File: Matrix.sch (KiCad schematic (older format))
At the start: 116 parts

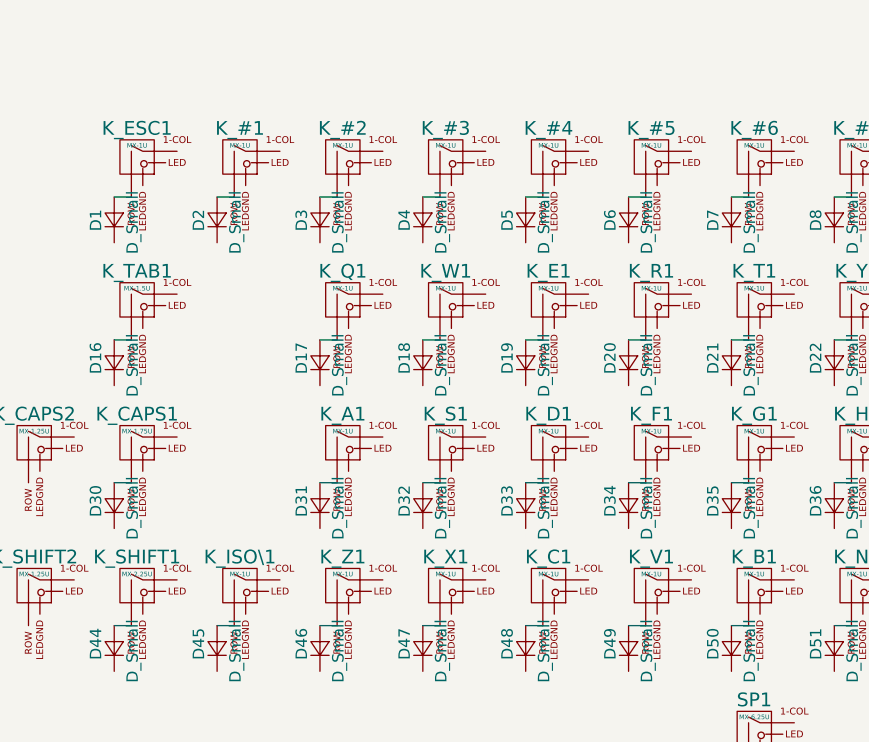
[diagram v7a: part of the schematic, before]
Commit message: Remove alps row
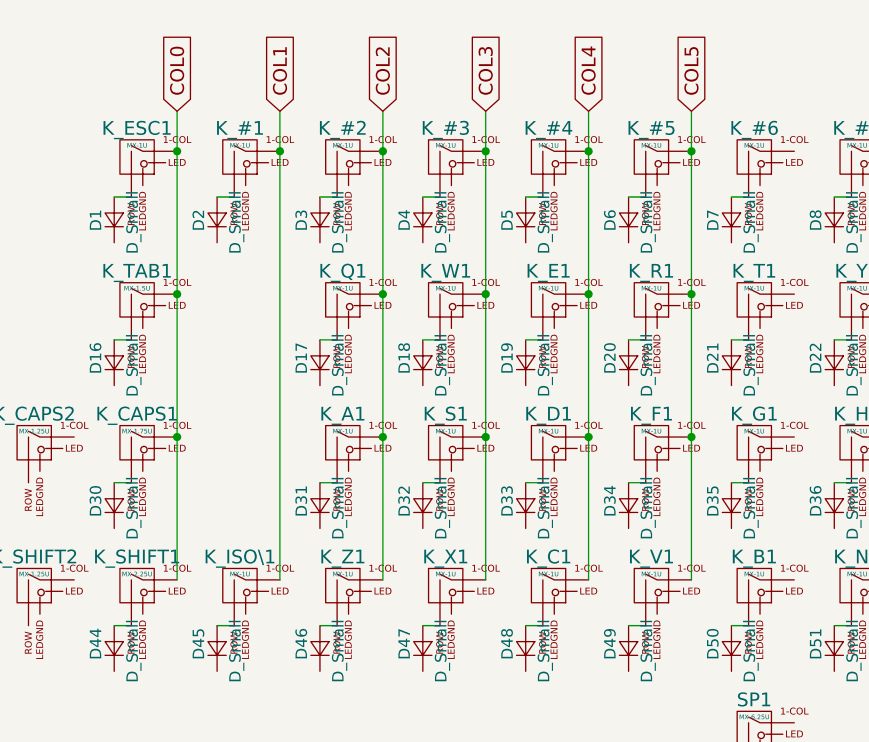
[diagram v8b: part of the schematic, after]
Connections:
- net COL0: now reaches K_ESC1.1 (COL)
- net COL0: now also K_CAPS1.1 (COL), K_SHIFT1.1 (COL), K_TAB1.1 (COL)
- net COL1: now reaches K_#1.1 (COL)
- net COL1: now also K_ISO\1.1 (COL)
- net COL2: now reaches K_#2.1 (COL)
- net COL2: now also K_A1.1 (COL), K_Q1.1 (COL), K_Z1.1 (COL)
- net COL3: now reaches K_#3.1 (COL)
- net COL3: now also K_S1.1 (COL), K_W1.1 (COL), K_X1.1 (COL)
- net COL4: now reaches K_#4.1 (COL)
- net COL4: now also K_C1.1 (COL), K_D1.1 (COL), K_E1.1 (COL)
- net COL5: now reaches K_#5.1 (COL)
- net COL5: now also K_F1.1 (COL), K_R1.1 (COL), K_V1.1 (COL)
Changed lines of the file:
@@
 	1    0    0    -1
 $EndComp
+Wire Wire Line
+	1675 1025 1675 3075
+Connection ~ 1675 2450
+Connection ~ 1675 1825
+Connection ~ 1675 1200
+Text GLabel 1675 1025 1    60   Input ~ 0
+COL0
+Wire Wire Line
+	2125 1025 2125 3075
+Text GLabel 2125 1025 1    60   Input ~ 0
+COL1
+Connection ~ 2125 1200
+Wire Wire Line
+	2575 1025 2575 3075
+Connection ~ 2575 1825
+Connection ~ 2575 2450
+Connection ~ 2575 1200
+Text GLabel 2575 1025 1    60   Input ~ 0
+COL2
+Wire Wire Line
+	3025 1025 3025 3075
+Text GLabel 3025 1025 1    60   Input ~ 0
+COL3
+Connection ~ 3025 1200
+Connection ~ 3025 1825
+Connection ~ 3025 2450
+Wire Wire Line
+	3475 1025 3475 3075
+Connection ~ 3475 2450
+Connection ~ 3475 1825
+Connection ~ 3475 1200
+Text GLabel 3475 1025 1    60   Input ~ 0
+COL4
+Wire Wire Line
+	3925 1025 3925 3075
+Text GLabel 3925 1025 1    60   Input ~ 0
+COL5
+Connection ~ 3925 1200
+Connection ~ 3925 1825
+Connection ~ 3925 2450
 $EndSCHEMATC
